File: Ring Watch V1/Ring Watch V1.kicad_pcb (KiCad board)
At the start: 2 copper layers, 24.1 x 25.4 mm, 13 parts, among them J1 Programming Header, J2 CR2023 Socket, U1 ATtiny85-20SU, U2 PCF8523T, Y1 32.768

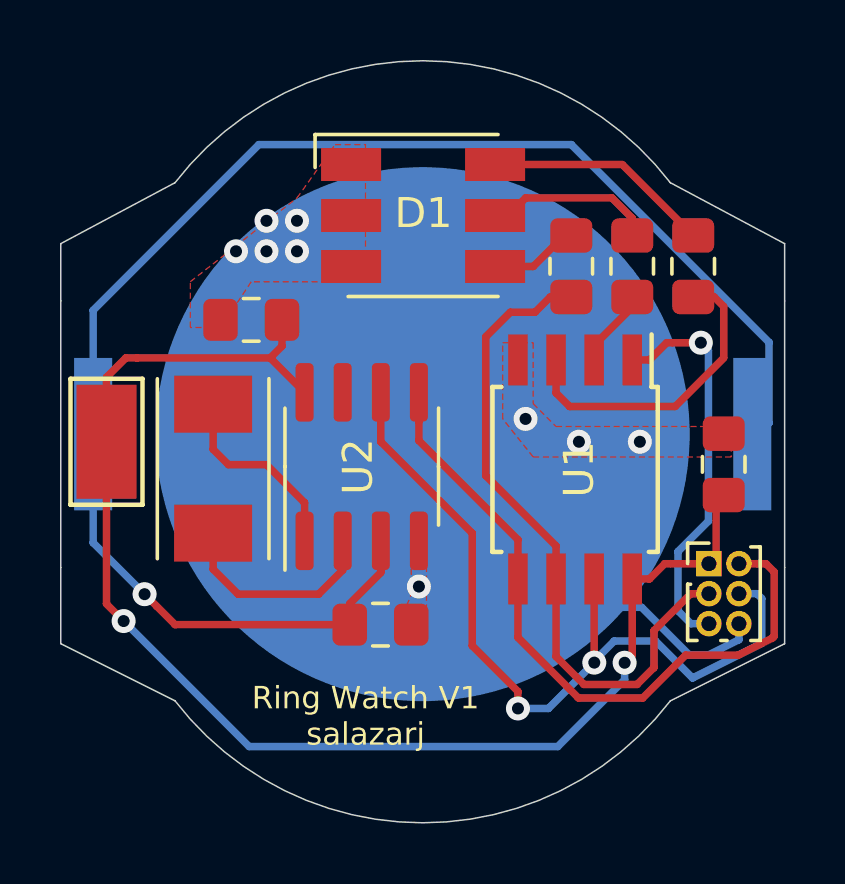
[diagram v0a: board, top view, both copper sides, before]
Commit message: added i2c pullups
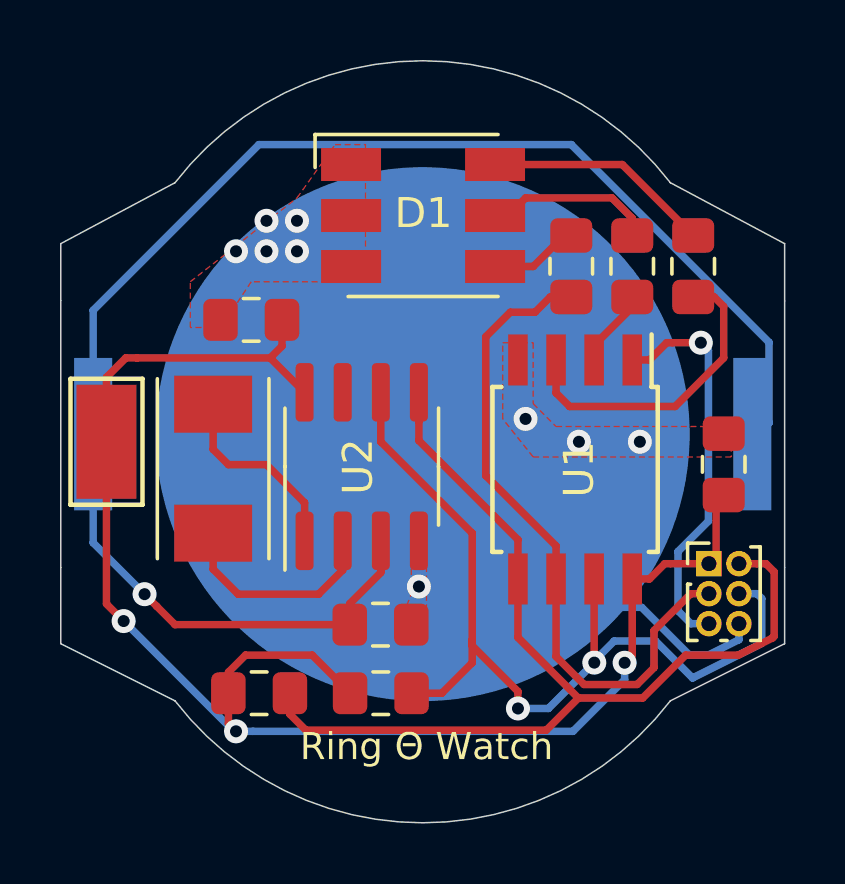
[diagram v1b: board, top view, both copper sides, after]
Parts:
- added R4: 10k, Resistor_SMD:R_0805_2012Metric_Pad1.15x1.40mm_HandSolder, F.Cu at (93.0, 116.6)
- added R5: 10k, Resistor_SMD:R_0805_2012Metric_Pad1.15x1.40mm_HandSolder, F.Cu at (97.0, 116.6)
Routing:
- net B0: track 23.1 -> 34.1 mm
- net Net-(C1-Pad1): track 44.0 -> 50.5 mm, vias 2 -> 3
- net B2: track 27.4 -> 30.6 mm
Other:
- board text added: "Ring Θ Watch"
- board text removed: "Ring Watch V1 salazarj"
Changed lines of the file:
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@@
     (thickness 1.6)
     (drawings 13)
-    (tracks 144)
+    (tracks 162)
     (zones 0)
-    (modules 13)
+    (modules 15)
     (nets 16)
   )
@@
     (add_net "Net-(U2-Pad7)")
   )
+  (module Resistor_SMD:R_0805_2012Metric_Pad1.15x1.40mm_HandSolder (layer F.Cu)
+    (at 97.028 116.586 180)
+    (descr "Resistor SMD 0805 (2012 Metric), square (rectangular) end terminal, IPC_7351 nominal with elongated pad for handsoldering. (Body size source: https://docs.google.com/spreadsheets/d/1BsfQQcO9C6DZCsRaXUlFlo91Tg2WpOkGARC1WS5S8t0/edit?usp=sharing), generated with kicad-footprint-generator")
+    (tags "resistor handsolder")
+    (attr smd)
+    (fp_text reference R5 (at 0 -1.65) (layer F.SilkS) hide
+      (effects (font (size 1 1) (thickness 0.15)))
+    )
+    (fp_text value 10k (at 0 1.65) (layer F.Fab)
+      (effects (font (size 1 1) (thickness 0.15)))
+    )
+    (fp_text user %R (at 0 0) (layer F.Fab)
+      (effects (font (size 0.5 0.5) (thickness 0.08)))
+    )
+    (fp_line (start 1.85 0.95) (end -1.85 0.95) (layer F.CrtYd) (width 0.05))
+    (fp_line (start 1.85 -0.95) (end 1.85 0.95) (layer F.CrtYd) (width 0.05))
+    (fp_line (start -1.85 -0.95) (end 1.85 -0.95) (layer F.CrtYd) (width 0.05))
+    (fp_line (start -1.85 0.95) (end -1.85 -0.95) (layer F.CrtYd) (width 0.05))
+    (fp_line (start -0.261252 0.71) (end 0.261252 0.71) (layer F.SilkS) (width 0.12))
+    (fp_line (start -0.261252 -0.71) (end 0.261252 -0.71) (layer F.SilkS) (width 0.12))
+    (fp_line (start 1 0.6) (end -1 0.6) (layer F.Fab) (width 0.1))
+    (fp_line (start 1 -0.6) (end 1 0.6) (layer F.Fab) (width 0.1))
+    (fp_line (start -1 -0.6) (end 1 -0.6) (layer F.Fab) (width 0.1))
+    (fp_line (start -1 0.6) (end -1 -0.6) (layer F.Fab) (width 0.1))
+    (pad 2 smd roundrect (at 1.025 0 180) (size 1.15 1.4) (layers F.Cu F.Paste F.Mask) (roundrect_rratio 0.217391)
+      (net 15 "Net-(C1-Pad1)"))
+    (pad 1 smd roundrect (at -1.025 0 180) (size 1.15 1.4) (layers F.Cu F.Paste F.Mask) (roundrect_rratio 0.217391)
+      (net 8 B2))
+    (model ${KISYS3DMOD}/Resistor_SMD.3dshapes/R_0805_2012Metric.wrl
+      (at (xyz 0 0 0))
+      (scale (xyz 1 1 1))
+      (rotate (xyz 0 0 0))
+    )
+  )
+  (module Resistor_SMD:R_0805_2012Metric_Pad1.15x1.40mm_HandSolder (layer F.Cu)
+    (at 92.973 116.586 180)
+    (descr "Resistor SMD 0805 (2012 Metric), square (rectangular) end terminal, IPC_7351 nominal with elongated pad for handsoldering. (Body size source: https://docs.google.com/spreadsheets/d/1BsfQQcO9C6DZCsRaXUlFlo91Tg2WpOkGARC1WS5S8t0/edit?usp=sharing), generated with kicad-footprint-generator")
+    (tags "resistor handsolder")
+    (attr smd)
+    (fp_text reference R4 (at 0 -1.65) (layer F.SilkS) hide
+      (effects (font (size 1 1) (thickness 0.15)))
+    )
+    (fp_text value 10k (at 0 1.65) (layer F.Fab) hide
+      (effects (font (size 1 1) (thickness 0.15)))
+    )
+    (fp_text user %R (at 0 0) (layer F.Fab)
+      (effects (font (size 0.5 0.5) (thickness 0.08)))
+    )
+    (fp_line (start 1.85 0.95) (end -1.85 0.95) (layer F.CrtYd) (width 0.05))
+    (fp_line (start 1.85 -0.95) (end 1.85 0.95) (layer F.CrtYd) (width 0.05))
+    (fp_line (start -1.85 -0.95) (end 1.85 -0.95) (layer F.CrtYd) (width 0.05))
+    (fp_line (start -1.85 0.95) (end -1.85 -0.95) (layer F.CrtYd) (width 0.05))
+    (fp_line (start -0.261252 0.71) (end 0.261252 0.71) (layer F.SilkS) (width 0.12))
+    (fp_line (start -0.261252 -0.71) (end 0.261252 -0.71) (layer F.SilkS) (width 0.12))
+    (fp_line (start 1 0.6) (end -1 0.6) (layer F.Fab) (width 0.1))
+    (fp_line (start 1 -0.6) (end 1 0.6) (layer F.Fab) (width 0.1))
+    (fp_line (start -1 -0.6) (end 1 -0.6) (layer F.Fab) (width 0.1))
+    (fp_line (start -1 0.6) (end -1 -0.6) (layer F.Fab) (width 0.1))
+    (pad 2 smd roundrect (at 1.025 0 180) (size 1.15 1.4) (layers F.Cu F.Paste F.Mask) (roundrect_rratio 0.217391)
+      (net 15 "Net-(C1-Pad1)"))
+    (pad 1 smd roundrect (at -1.025 0 180) (size 1.15 1.4) (layers F.Cu F.Paste F.Mask) (roundrect_rratio 0.217391)
+      (net 6 B0))
+    (model ${KISYS3DMOD}/Resistor_SMD.3dshapes/R_0805_2012Metric.wrl
+      (at (xyz 0 0 0))
+      (scale (xyz 1 1 1))
+      (rotate (xyz 0 0 0))
+    )
+  )
   (module Capacitor_SMD:C_0805_2012Metric_Pad1.15x1.40mm_HandSolder (layer F.Cu)
     (at 92.71 104.14 180)
@@
     )
   )
-  (gr_text "Ring Watch V1\nsalazarj" (at 96.52 117.348) (layer F.SilkS)
-    (effects (font (size 0.75 0.75) (thickness 0.1875)))
+  (gr_text "Ring Θ Watch\n" (at 98.552 118.364) (layer F.SilkS)
+    (effects (font (size 0.9 0.9) (thickness 0.225)))
   )
   (gr_line (start 110.49 103.505001) (end 110.489998 112.394999) (layer Edge.Cuts) (width 0.05))
@@
   (segment (start 105.758989 116.745011) (end 107.188 115.316) (width 0.25) (layer F.Cu) (net 6))
   (segment (start 103.614919 116.745011) (end 105.758989 116.745011) (width 0.25) (layer F.Cu) (net 6))
+  (segment (start 93.998 116.586) (end 93.998 117.286) (width 0.25) (layer F.Cu) (net 6))
+  (segment (start 93.998 117.286) (end 94.531001 117.819001) (width 0.25) (layer F.Cu) (net 6))
+  (segment (start 102.540929 117.819001) (end 103.614919 116.745011) (width 0.25) (layer F.Cu) (net 6))
+  (segment (start 94.531001 117.819001) (end 102.540929 117.819001) (width 0.25) (layer F.Cu) (net 6))
   (segment (start 102.678 103.378) (end 102.17 103.886) (width 0.25) (layer F.Cu) (net 7))
   (segment (start 103.378 103.378) (end 102.678 103.378) (width 0.25) (layer F.Cu) (net 7))
@@
   (segment (start 97.028 108.204) (end 97.028 106.556) (width 0.25) (layer F.Cu) (net 8))
   (segment (start 100.076 111.252) (end 97.028 108.204) (width 0.25) (layer F.Cu) (net 8))
-  (segment (start 100.076 115.004315) (end 100.076 111.252) (width 0.25) (layer F.Cu) (net 8))
   (segment (start 101.6 117.094) (end 101.6 116.528315) (width 0.25) (layer F.Cu) (net 8))
-  (segment (start 101.6 116.528315) (end 100.076 115.004315) (width 0.25) (layer F.Cu) (net 8))
   (via (at 104.14466 115.56534) (size 0.8) (drill 0.4) (layers F.Cu B.Cu) (net 8))
   (segment (start 104.14466 115.508338) (end 104.14466 115.56534) (width 0.25) (layer B.Cu) (net 8))
@@
   (segment (start 104.807999 114.844999) (end 104.14466 115.508338) (width 0.25) (layer B.Cu) (net 8))
   (segment (start 109.56704 113.268) (end 109.728 113.42896) (width 0.25) (layer B.Cu) (net 8))
+  (segment (start 101.6 116.528315) (end 100.076 115.004315) (width 0.25) (layer F.Cu) (net 8))
+  (segment (start 100.076 114.808) (end 100.076 111.252) (width 0.25) (layer F.Cu) (net 8))
+  (segment (start 100.076 114.808) (end 100.076 115.57) (width 0.25) (layer F.Cu) (net 8))
+  (segment (start 100.076 115.004315) (end 100.076 114.808) (width 0.25) (layer F.Cu) (net 8))
+  (segment (start 99.06 116.586) (end 98.053 116.586) (width 0.25) (layer F.Cu) (net 8))
+  (segment (start 100.076 115.57) (end 99.06 116.586) (width 0.25) (layer F.Cu) (net 8))
   (segment (start 105.41 103.715998) (end 105.41 103.378) (width 0.25) (layer F.Cu) (net 9))
   (segment (start 104.14 104.985998) (end 105.41 103.715998) (width 0.25) (layer F.Cu) (net 9))
@@
   (via (at 105.155998 115.57) (size 0.8) (drill 0.4) (layers F.Cu B.Cu) (net 15))
   (segment (start 105.41 112.776) (end 105.41 115.315998) (width 0.25) (layer F.Cu) (net 15))
-  (segment (start 88.456284 114.180181) (end 92.640103 118.364) (width 0.25) (layer B.Cu) (net 15))
   (segment (start 105.41 115.315998) (end 105.155998 115.57) (width 0.25) (layer F.Cu) (net 15))
-  (segment (start 92.640103 118.364) (end 102.927683 118.364) (width 0.25) (layer B.Cu) (net 15))
-  (segment (start 105.155998 116.135685) (end 105.155998 115.57) (width 0.25) (layer B.Cu) (net 15))
-  (segment (start 102.927683 118.364) (end 105.155998 116.135685) (width 0.25) (layer B.Cu) (net 15))
+  (segment (start 96.003 116.577) (end 96.003 116.586) (width 0.25) (layer F.Cu) (net 15))
+  (segment (start 92.518 115.316) (end 94.742 115.316) (width 0.25) (layer F.Cu) (net 15))
+  (segment (start 94.742 115.316) (end 96.003 116.577) (width 0.25) (layer F.Cu) (net 15))
+  (segment (start 91.948 116.586) (end 91.948 115.886) (width 0.25) (layer F.Cu) (net 15))
+  (segment (start 91.948 115.886) (end 92.518 115.316) (width 0.25) (layer F.Cu) (net 15))
+  (segment (start 92.767685 117.856) (end 92.202 117.856) (width 0.25) (layer B.Cu) (net 15))
+  (via (at 92.202 117.856) (size 0.8) (drill 0.4) (layers F.Cu B.Cu) (net 15))
+  (segment (start 91.948 116.586) (end 91.948 117.602) (width 0.25) (layer F.Cu) (net 15))
+  (segment (start 105.155998 115.57) (end 105.155998 116.135685) (width 0.25) (layer B.Cu) (net 15))
+  (segment (start 103.435683 117.856) (end 92.767685 117.856) (width 0.25) (layer B.Cu) (net 15))
+  (segment (start 105.155998 116.135685) (end 103.435683 117.856) (width 0.25) (layer B.Cu) (net 15))
+  (segment (start 92.132103 117.856) (end 92.202 117.856) (width 0.25) (layer B.Cu) (net 15))
+  (segment (start 88.456284 114.180181) (end 92.132103 117.856) (width 0.25) (layer B.Cu) (net 15))
+  (segment (start 91.948 117.602) (end 92.202 117.856) (width 0.25) (layer F.Cu) (net 15))
   (zone (net 2) (net_name GND) (layer F.Cu) (hatch edge 0.508)
     (priority 1)

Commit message: changed crystal footprint, added preliminary BOMs
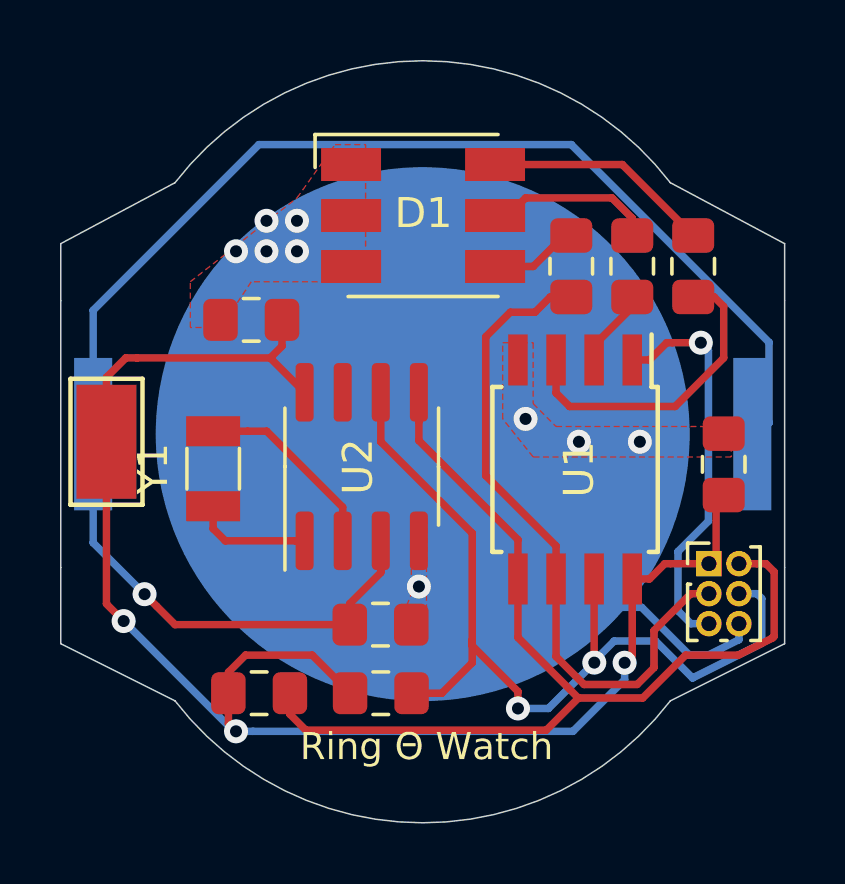
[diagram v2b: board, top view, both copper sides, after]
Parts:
- Y1: footprint Crystal:Crystal_SMD_Abracon_ABM7-2Pin_6.0x3.5mm -> Crystal:Crystal_SMD_3215-2Pin_3.2x1.5mm
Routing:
- net Net-(U2-Pad1): track 6.91 -> 3.97 mm
- net Net-(U2-Pad2): track 7.17 -> 6.49 mm
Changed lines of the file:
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@@
     (thickness 1.6)
     (drawings 13)
-    (tracks 162)
+    (tracks 159)
     (zones 0)
     (modules 15)
@@
       (outputformat 1)
       (mirror false)
-      (drillshape 1)
+      (drillshape 0)
       (scaleselection 1)
-      (outputdirectory ""))
+      (outputdirectory "12_31_20 Outputs/"))
   )
   (net 0 "")
@@
     (add_net "Net-(U2-Pad2)")
     (add_net "Net-(U2-Pad7)")
+  )
+  (module Crystal:Crystal_SMD_3215-2Pin_3.2x1.5mm (layer F.Cu)
+    (at 91.44 109.102 90)
+    (descr "SMD Crystal FC-135 https://support.epson.biz/td/api/doc_check.php?dl=brief_FC-135R_en.pdf")
+    (tags "SMD SMT Crystal")
+    (attr smd)
+    (fp_text reference Y1 (at 0 -2 90) (layer F.SilkS)
+      (effects (font (size 1 1) (thickness 0.15)))
+    )
+    (fp_text value 32.768 (at 0 2 90) (layer F.Fab)
+      (effects (font (size 1 1) (thickness 0.15)))
+    )
+    (fp_line (start 2 -1.15) (end 2 1.15) (layer F.CrtYd) (width 0.05))
+    (fp_line (start -2 -1.15) (end -2 1.15) (layer F.CrtYd) (width 0.05))
+    (fp_line (start -2 1.15) (end 2 1.15) (layer F.CrtYd) (width 0.05))
+    (fp_line (start -1.6 0.75) (end 1.6 0.75) (layer F.Fab) (width 0.1))
+    (fp_line (start -1.6 -0.75) (end 1.6 -0.75) (layer F.Fab) (width 0.1))
+    (fp_line (start 1.6 -0.75) (end 1.6 0.75) (layer F.Fab) (width 0.1))
+    (fp_line (start -0.675 -0.875) (end 0.675 -0.875) (layer F.SilkS) (width 0.12))
+    (fp_line (start -0.675 0.875) (end 0.675 0.875) (layer F.SilkS) (width 0.12))
+    (fp_line (start -1.6 -0.75) (end -1.6 0.75) (layer F.Fab) (width 0.1))
+    (fp_line (start -2 -1.15) (end 2 -1.15) (layer F.CrtYd) (width 0.05))
+    (fp_text user %R (at 0 -2 90) (layer F.Fab)
+      (effects (font (size 1 1) (thickness 0.15)))
+    )
+    (pad 2 smd rect (at -1.25 0 90) (size 1 1.8) (layers F.Cu F.Paste F.Mask)
+      (net 12 "Net-(U2-Pad1)"))
+    (pad 1 smd rect (at 1.25 0 90) (size 1 1.8) (layers F.Cu F.Paste F.Mask)
+      (net 13 "Net-(U2-Pad2)"))
+    (model ${KISYS3DMOD}/Crystal.3dshapes/Crystal_SMD_3215-2Pin_3.2x1.5mm.wrl
+      (at (xyz 0 0 0))
+      (scale (xyz 1 1 1))
+      (rotate (xyz 0 0 0))
+    )
   )
   (module Resistor_SMD:R_0805_2012Metric_Pad1.15x1.40mm_HandSolder (layer F.Cu)
@@
       (net 5 "Net-(D1-Pad6)"))
     (model ${KISYS3DMOD}/Resistor_SMD.3dshapes/R_0805_2012Metric.wrl
-      (at (xyz 0 0 0))
-      (scale (xyz 1 1 1))
-      (rotate (xyz 0 0 0))
-    )
-  )
-  (module Crystal:Crystal_SMD_Abracon_ABM7-2Pin_6.0x3.5mm (layer F.Cu)
-    (at 91.44 109.102 90)
-    (descr "SMD Crystal Abracon ABM7, https://abracon.com/Resonators/abm7.pdf")
-    (tags "SMD SMT crystal")
-    (attr smd)
-    (fp_text reference Y1 (at -4.318 0.127 180) (layer F.SilkS) hide
-      (effects (font (size 1 1) (thickness 0.15)))
-    )
-    (fp_text value 32.768 (at -0.762 2.667 90) (layer F.Fab)
-      (effects (font (size 1 1) (thickness 0.15)))
-    )
-    (fp_text user %R (at 4.318 -1.143 90) (layer F.Fab)
-      (effects (font (size 1 1) (thickness 0.15)))
-    )
-    (fp_line (start -3 -1.75) (end -3 1.75) (layer F.Fab) (width 0.1))
-    (fp_line (start -3 1.75) (end 3 1.75) (layer F.Fab) (width 0.1))
-    (fp_line (start 3 -1.75) (end 3 1.75) (layer F.Fab) (width 0.1))
-    (fp_line (start -3 -1.75) (end 3 -1.75) (layer F.Fab) (width 0.1))
-    (fp_line (start -3 -1.86) (end 3 -1.86) (layer F.SilkS) (width 0.12))
-    (fp_line (start -3 1.86) (end 3 1.86) (layer F.SilkS) (width 0.12))
-    (fp_line (start -3.35 -2) (end 3.35 -2) (layer F.CrtYd) (width 0.05))
-    (fp_line (start -3.35 -2) (end -3.35 2) (layer F.CrtYd) (width 0.05))
-    (fp_line (start 3.35 2) (end 3.35 -2) (layer F.CrtYd) (width 0.05))
-    (fp_line (start 3.35 2) (end -3.35 2) (layer F.CrtYd) (width 0.05))
-    (pad 1 smd rect (at -2.15 0 90) (size 1.9 2.6) (layers F.Cu F.Paste F.Mask)
-      (net 13 "Net-(U2-Pad2)"))
-    (pad 2 smd rect (at 2.15 0 90) (size 1.9 2.6) (layers F.Cu F.Paste F.Mask)
-      (net 12 "Net-(U2-Pad1)"))
-    (model ${KISYS3DMOD}/Crystal.3dshapes/Crystal_SMD_Abracon_ABM7-2Pin_6.0x3.5mm.wrl
       (at (xyz 0 0 0))
       (scale (xyz 1 1 1))
@@
   (segment (start 105.985 105.476) (end 106.559 104.902) (width 0.25) (layer F.Cu) (net 11))
   (segment (start 105.41 105.476) (end 105.985 105.476) (width 0.25) (layer F.Cu) (net 11))
-  (segment (start 91.44 106.444) (end 91.79 106.444) (width 0.25) (layer F.Cu) (net 12))
-  (segment (start 91.44 108.458) (end 91.948 108.966) (width 0.25) (layer F.Cu) (net 12))
-  (segment (start 91.44 106.952) (end 91.44 108.458) (width 0.25) (layer F.Cu) (net 12))
-  (segment (start 91.948 108.966) (end 93.218 108.966) (width 0.25) (layer F.Cu) (net 12))
-  (segment (start 94.488 110.236) (end 94.488 111.506) (width 0.25) (layer F.Cu) (net 12))
-  (segment (start 93.218 108.966) (end 94.488 110.236) (width 0.25) (layer F.Cu) (net 12))
-  (segment (start 94.955 113.284) (end 95.758 112.481) (width 0.25) (layer F.Cu) (net 13))
-  (segment (start 92.272 113.284) (end 94.955 113.284) (width 0.25) (layer F.Cu) (net 13))
-  (segment (start 95.758 112.481) (end 95.758 111.506) (width 0.25) (layer F.Cu) (net 13))
-  (segment (start 91.44 112.452) (end 92.272 113.284) (width 0.25) (layer F.Cu) (net 13))
-  (segment (start 91.44 111.252) (end 91.44 112.452) (width 0.25) (layer F.Cu) (net 13))
+  (segment (start 91.844 111.506) (end 94.188 111.506) (width 0.25) (layer F.Cu) (net 12))
+  (segment (start 94.188 111.506) (end 94.488 111.506) (width 0.25) (layer F.Cu) (net 12))
+  (segment (start 91.44 111.102) (end 91.844 111.506) (width 0.25) (layer F.Cu) (net 12))
+  (segment (start 91.44 110.352) (end 91.44 111.102) (width 0.25) (layer F.Cu) (net 12))
+  (segment (start 95.758 110.3835) (end 93.2265 107.852) (width 0.25) (layer F.Cu) (net 13))
+  (segment (start 95.758 111.506) (end 95.758 110.3835) (width 0.25) (layer F.Cu) (net 13))
+  (segment (start 92.59 107.852) (end 91.44 107.852) (width 0.25) (layer F.Cu) (net 13))
+  (segment (start 93.2265 107.852) (end 92.59 107.852) (width 0.25) (layer F.Cu) (net 13))
   (segment (start 107.966 112.268) (end 106.68 112.268) (width 0.25) (layer F.Cu) (net 15))
   (segment (start 108.204 109.982) (end 108.204 112.03) (width 0.25) (layer F.Cu) (net 15))
